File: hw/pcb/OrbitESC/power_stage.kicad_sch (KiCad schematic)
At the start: 49 parts, among them U13 TLV9051IDBVR, U14 TLV9051IDBVR, U4 TLV9051IDBVR, U5 DRV8300DRGER, U6 TLV9051IDBVR

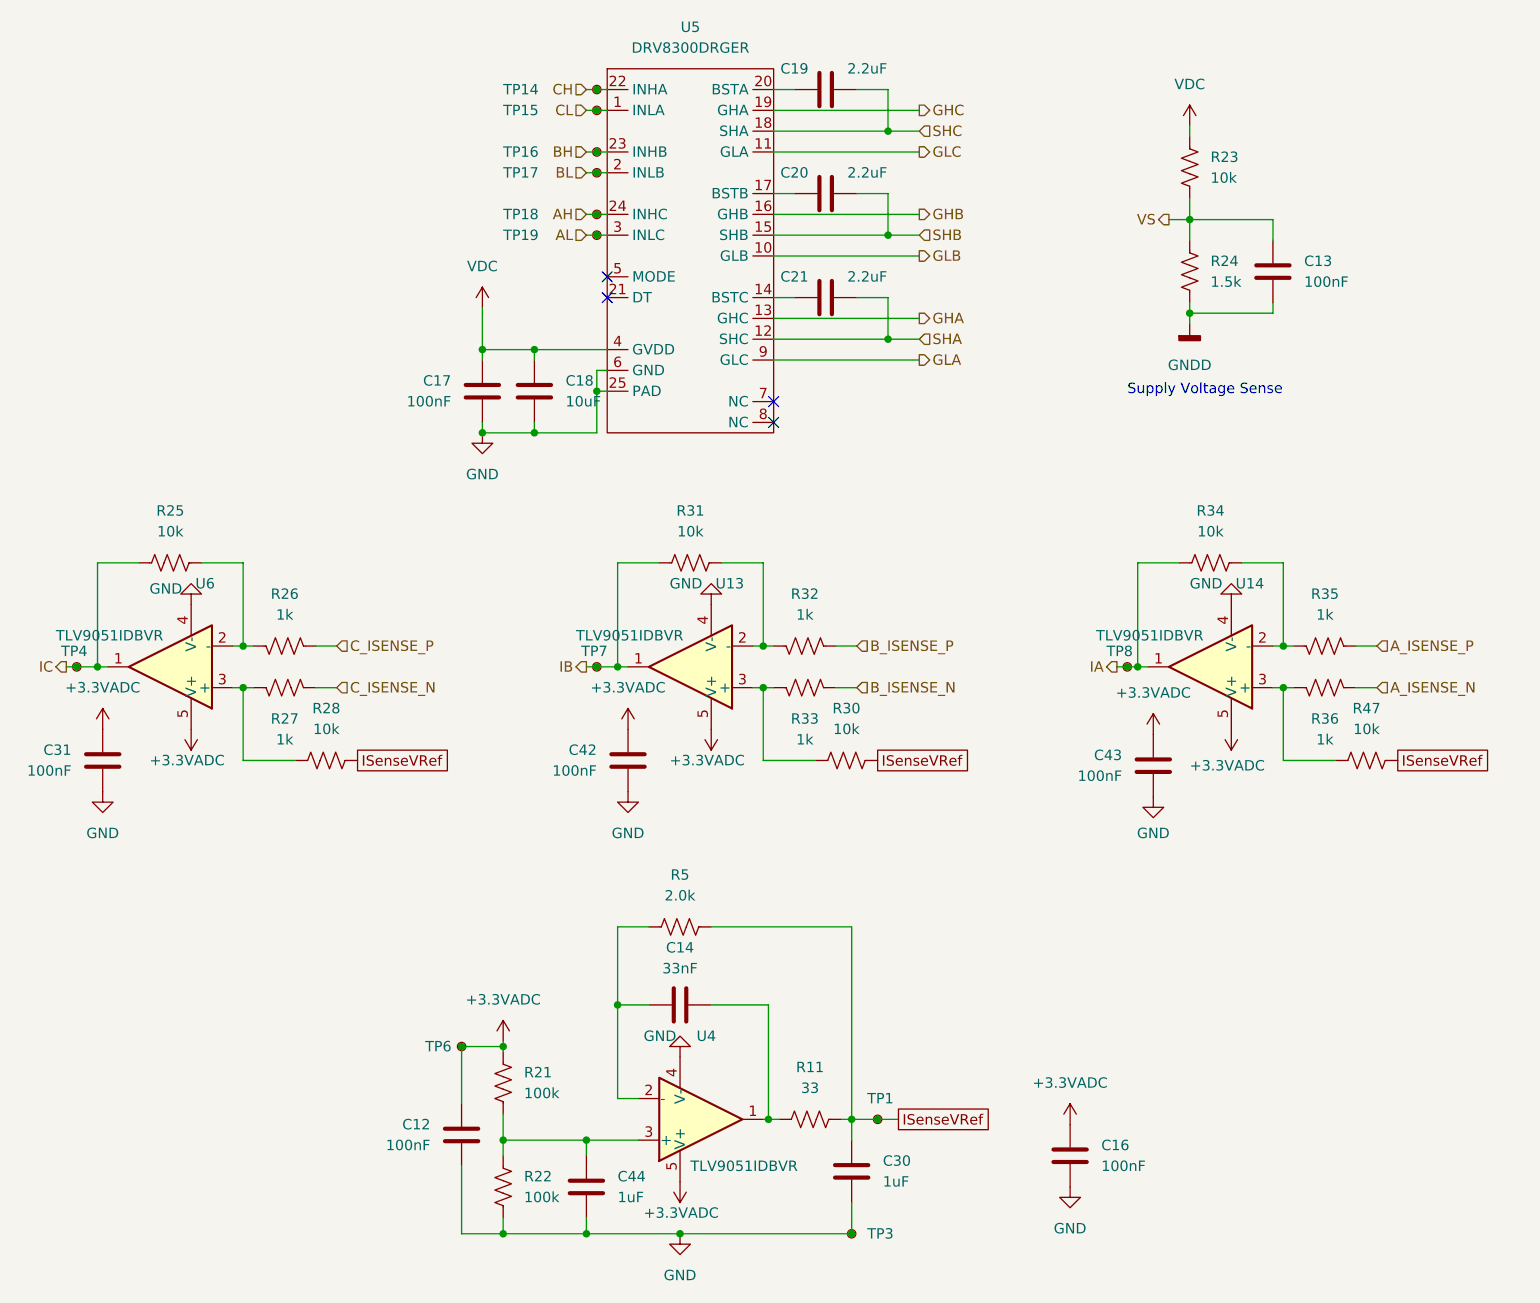
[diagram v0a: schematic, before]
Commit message: Update PCB to fix comparator pin swap
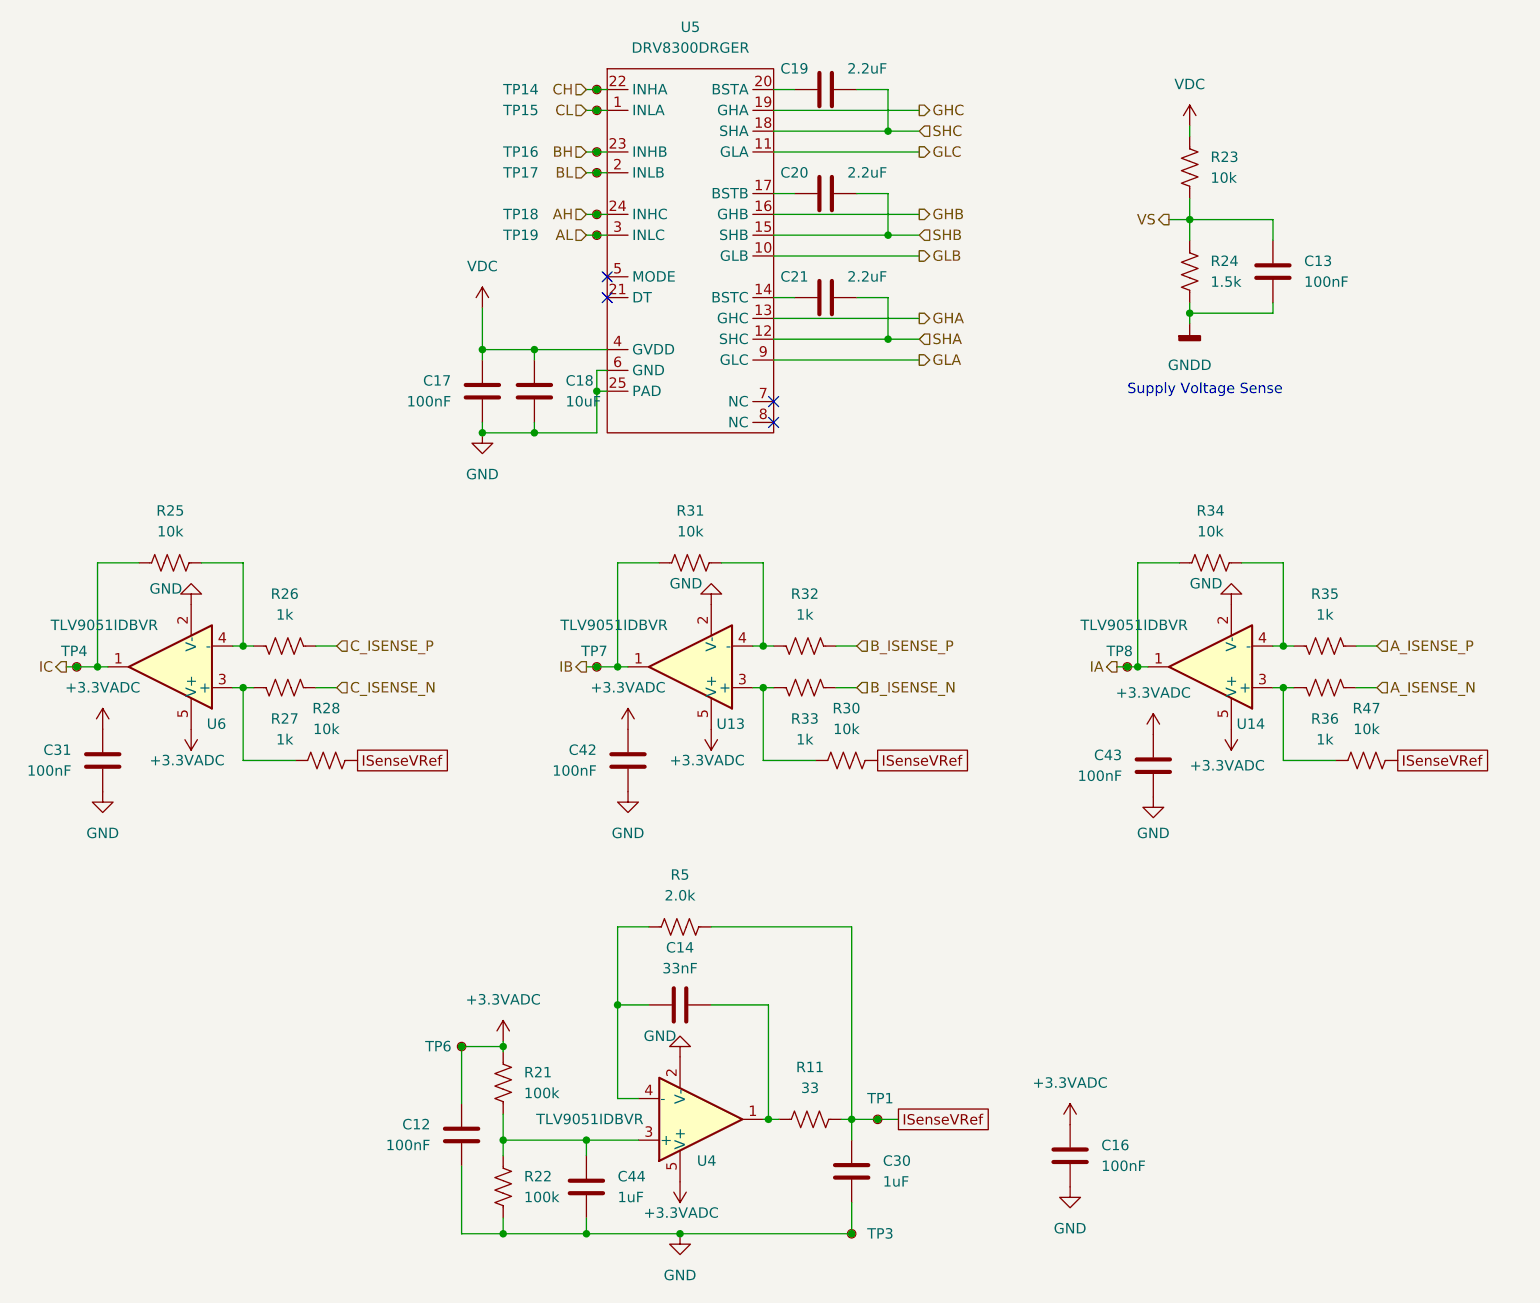
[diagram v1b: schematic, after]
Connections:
- net GND: now also U13.2 (V-), U14.2 (V-), U4.2 (V-), U6.2 (V-); no longer U13.4 (V-), U14.4 (V-), U4.4 (V-), U6.4 (V-)
- net at R25.2, R26.2: now also U6.4 (-); no longer U6.2 (-)
- net at C14.1, R5.2: now also U4.4 (-); no longer U4.2 (-)
- net at R34.2, R35.2: now also U14.4 (-); no longer U14.2 (-)
- net at R31.2, R32.2: now also U13.4 (-); no longer U13.2 (-)
